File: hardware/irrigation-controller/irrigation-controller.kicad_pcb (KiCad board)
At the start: 2 copper layers, 109 x 71.6 mm, 83 parts, among them J1 RS485, J10 I2C, J11 IO, J12 RELAY_2, J15 FLOW_1, J2 I2C, J3 ICSP, J4 UART, J5 RF Module, J6 PWR 24V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

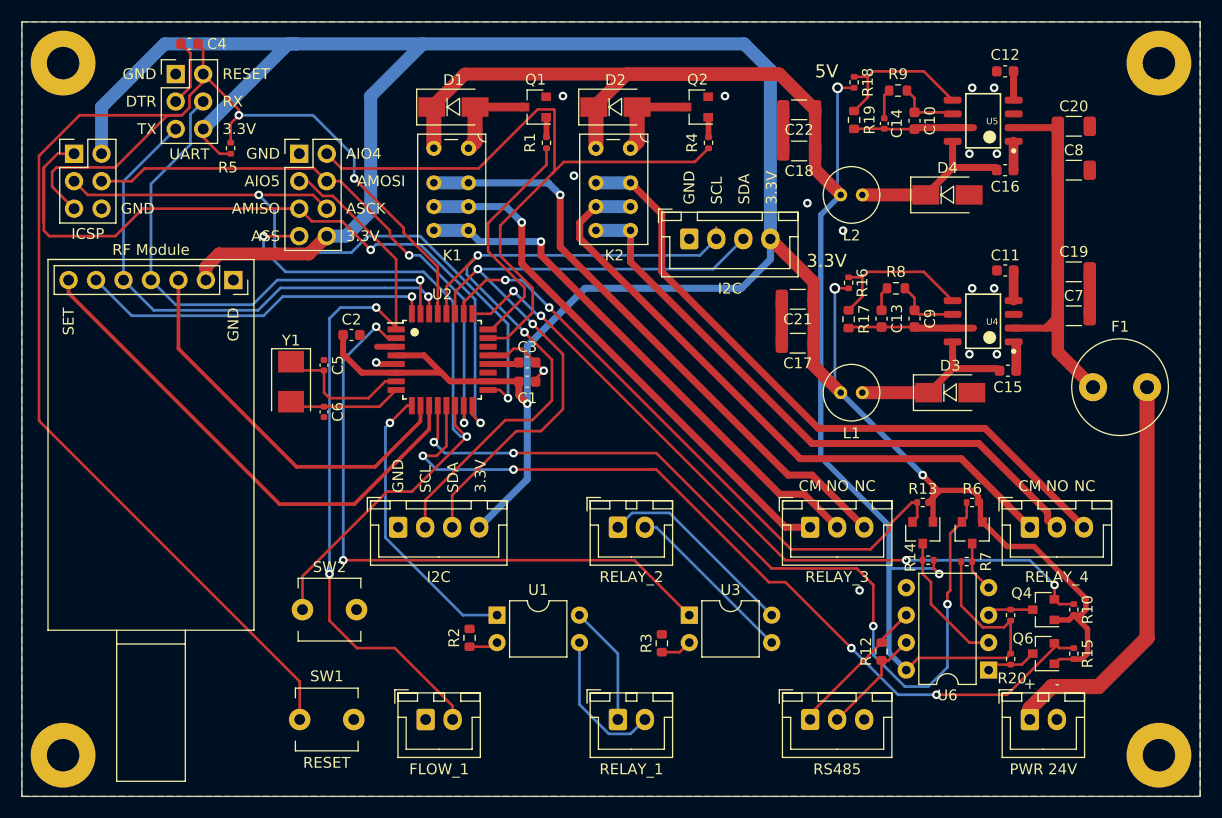
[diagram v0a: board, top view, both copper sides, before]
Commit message: Increase clearance for controller board
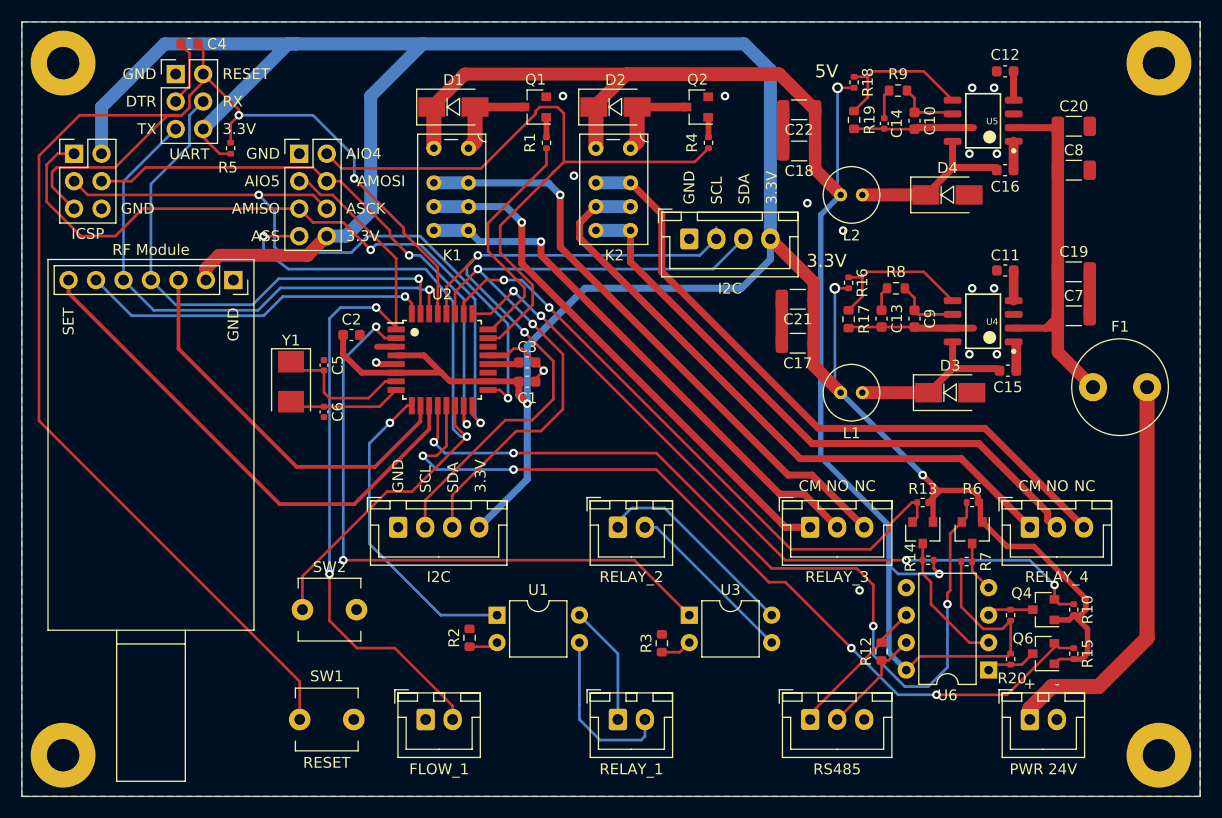
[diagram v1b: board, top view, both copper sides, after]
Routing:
- net AMISO: track 72.8 -> 65.8 mm
- net AIO1: track 26.8 -> 29.2 mm
- net R1B: track 13.4 -> 15.7 mm
- net +5V: track 162.4 -> 163.3 mm
- net R2A: track 18.7 -> 19.4 mm
- net AMOSI: track 52.4 -> 52.9 mm
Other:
- net class Default: clearance 0.2 -> 0.25
- rule trace_clearance: 0.2 -> 0.25
- rule trace_min: 0.2 -> 0.25

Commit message: Add controller board author name
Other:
- board text added: "Designed by Daniel McMillan - 2021"

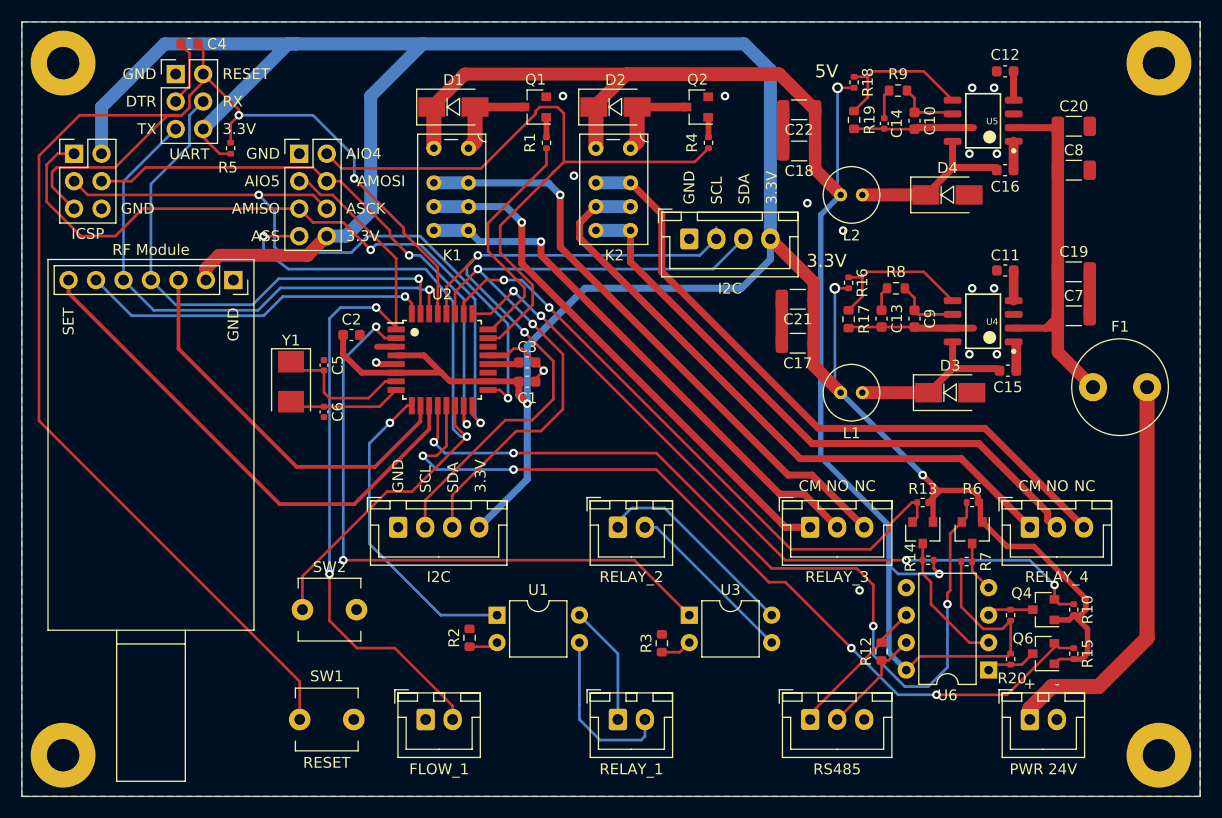
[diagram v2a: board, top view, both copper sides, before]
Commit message: Add avocado image to controller board
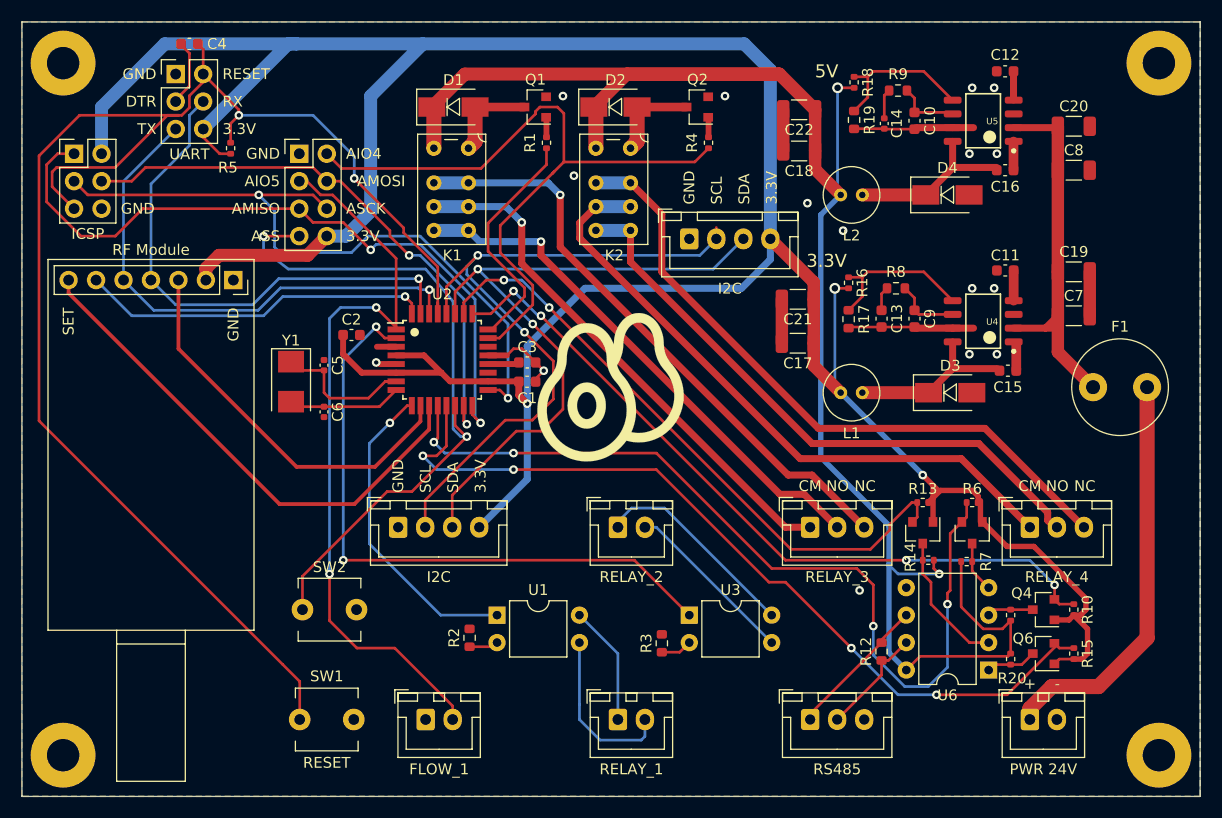
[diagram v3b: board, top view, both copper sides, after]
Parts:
- added G***: LOGO, lib:avocado, F.Cu at (106.0, 111.5)
